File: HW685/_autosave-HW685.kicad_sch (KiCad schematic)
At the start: 34 parts, among them J1 Screw_Terminal_01x03, J2 Screw_Terminal_01x02, U1 ICL7660, U2 LM317L_TO92, U3 TL431, U4 LM358

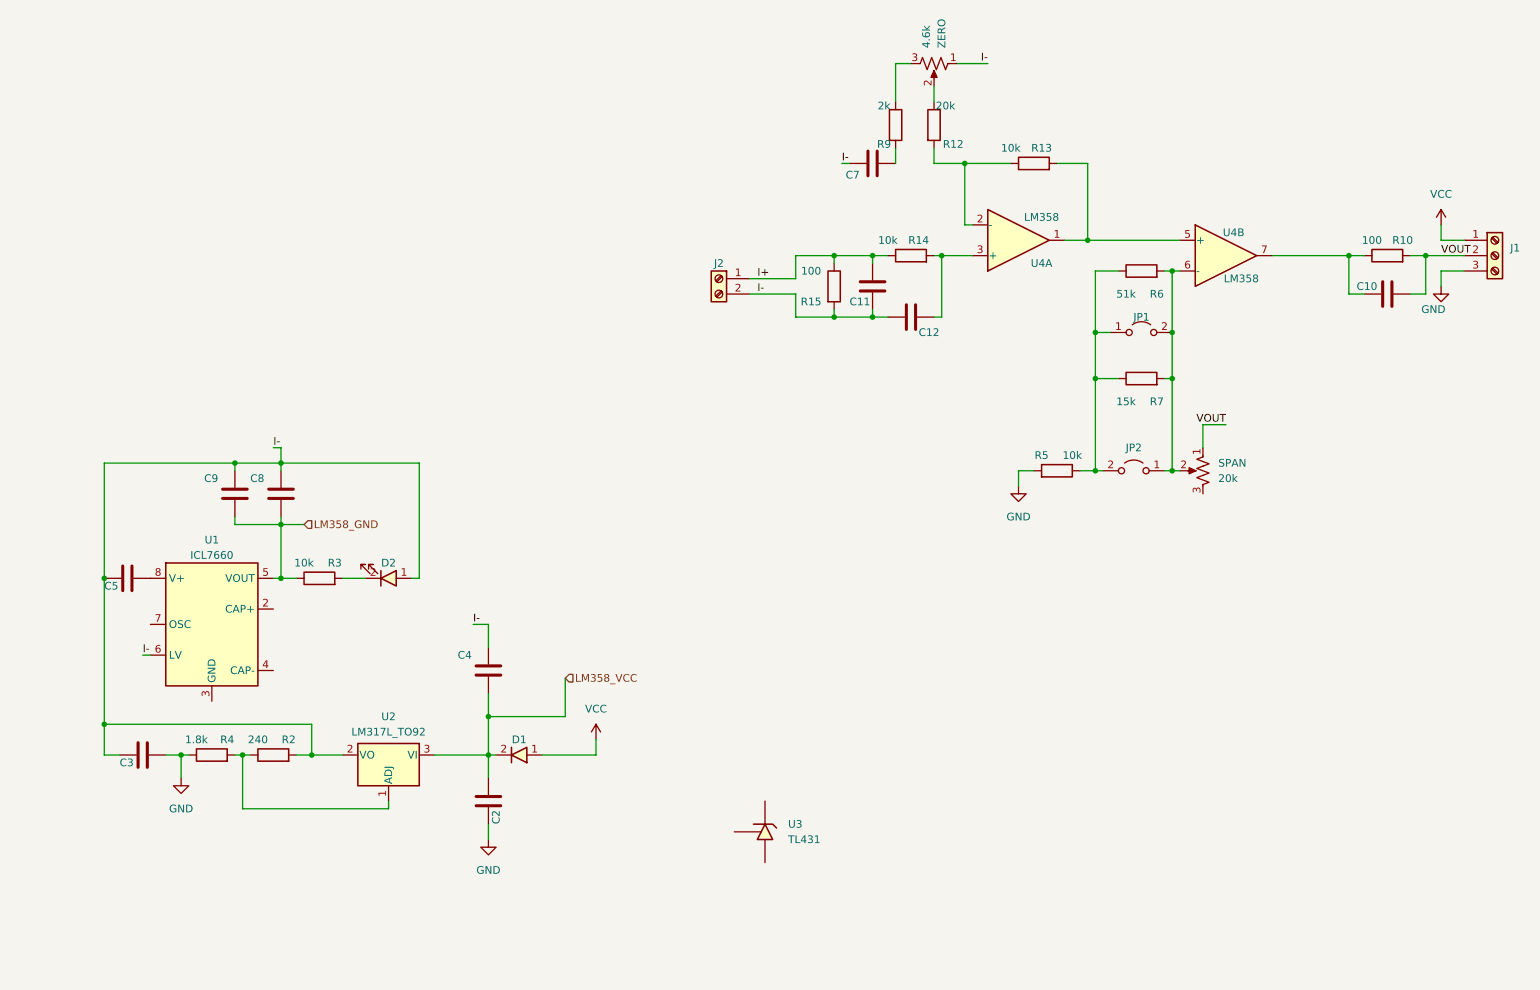
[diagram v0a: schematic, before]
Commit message: Complete HW-685 Schematic
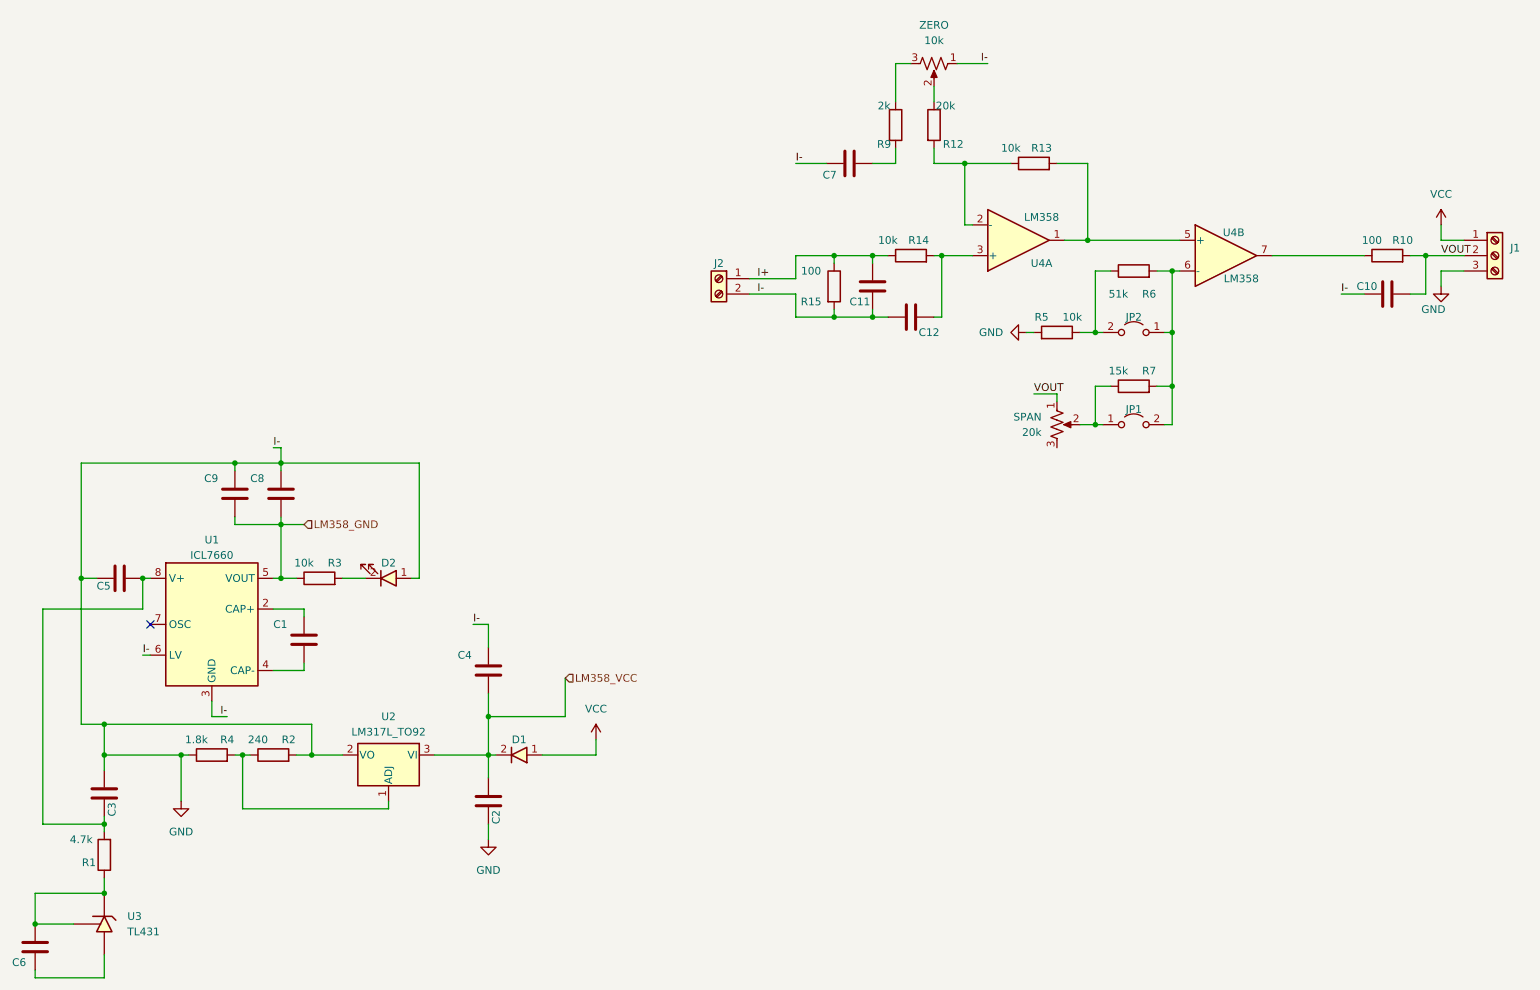
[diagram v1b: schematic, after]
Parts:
- added C1, C6: 10uF, symbol Device:C
- added R1: 4.7k, symbol Device:R
- ZERO: value 4.6k -> 10k
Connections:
- net GND: now also C10.2, C11.2, C12.2, C4.1, C5.2, C7.2, C8.1, C9.1, D2.1, J2.2 (Pin_2), R15.2, R2.2, U1.3 (GND), U1.6 (LV), U2.2 (VO), ZERO.1
- net at JP1.2 (B), JP2.1 (A), R6.2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: no longer SPAN.2
- net at JP2.2 (B), R5.1, R6.1: no longer JP1.1 (A), R7.1
- net at U1.2 (CAP+): now also C1.1
- net at U1.4 (CAP-): now also C1.2
- net at C5.1, U1.8 (V+): now also C3.2, R1.2
- net at U3.1 (K): now also U3.2 (REF), C6.1, R1.1
- net at U3.3 (A): now also C6.2
- net at R10.1, U4.7: no longer C10.2
- removed net I-: C11.2, C12.2, C3.2, C4.1, C5.2, C7.2, C8.1, C9.1, D2.1, J2.2 (Pin_2), R15.2, R2.2, U1.6 (LV), U2.2 (VO), ZERO.1
- new net: JP1.1 (A), R7.1, SPAN.2
- no-connect marks 0 -> 1
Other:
- moved on the sheet: C3, C5, C7, JP1, JP2, R5, R6, R7, SPAN, U3
